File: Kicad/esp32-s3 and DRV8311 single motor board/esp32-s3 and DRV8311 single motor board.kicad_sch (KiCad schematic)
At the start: 41 parts, among them J1 JST SH SM04B, J2 JST SH SM06B, J4 Conn_01x02_Pin, SW1 SW_Push, U5 ESP32-S3, Y1 40mhz

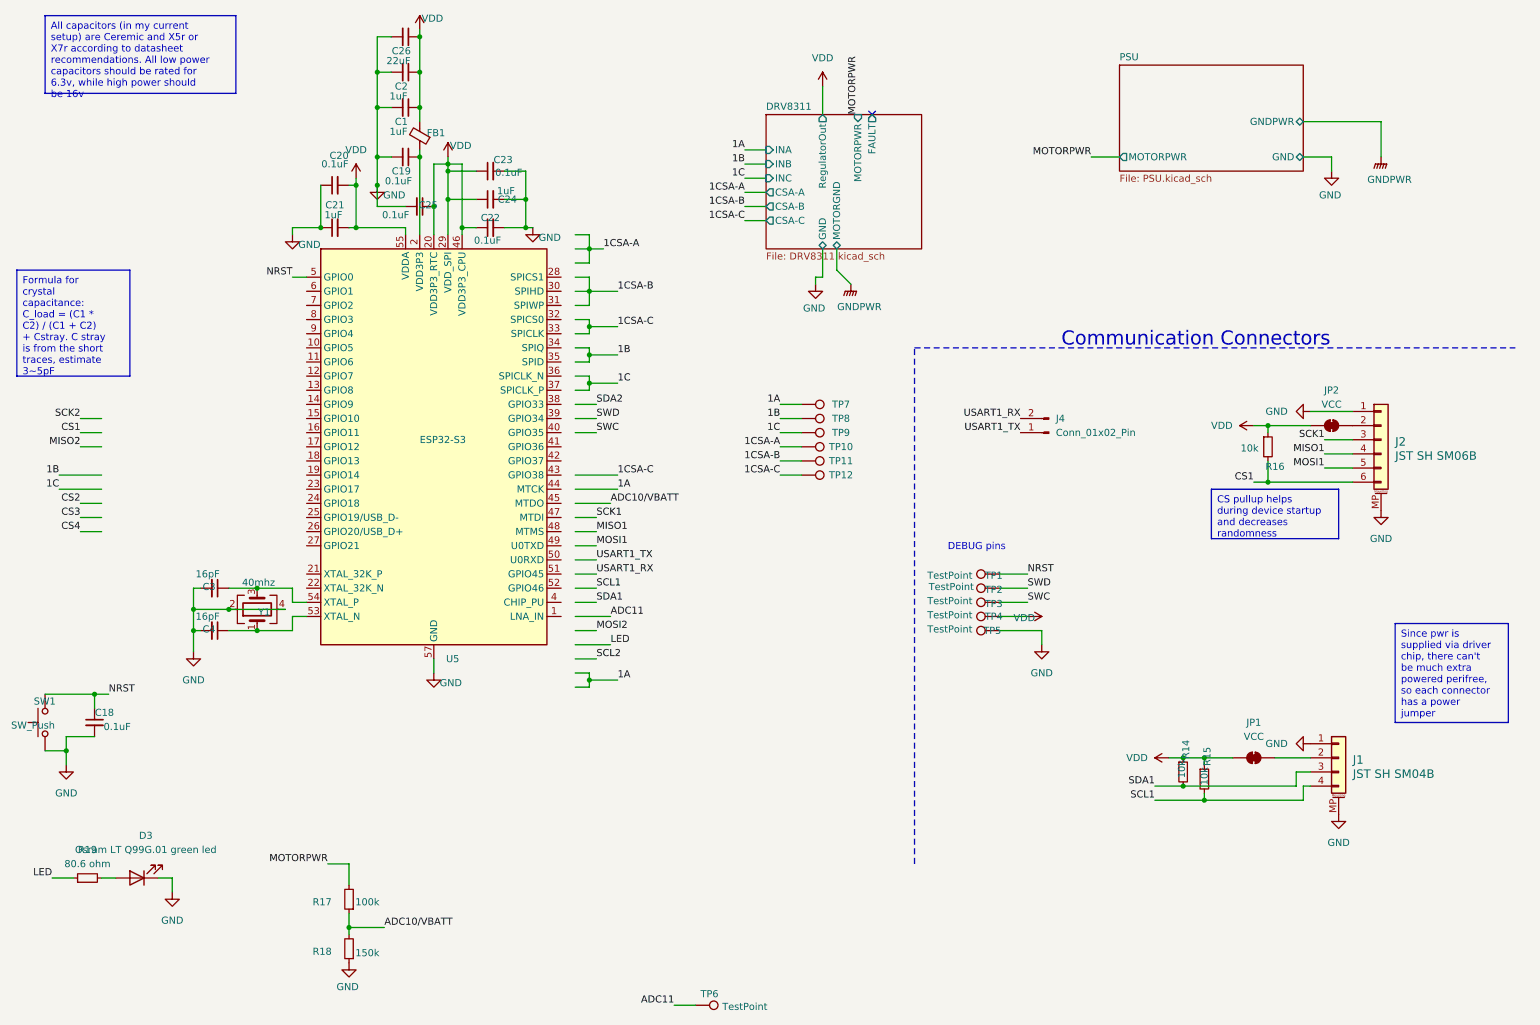
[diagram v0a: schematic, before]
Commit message: Mostly finished draft wiring
I added test points to practically every pin I won't be using regularly. Even if I never use a pin, it is better to have it exposed somehow than to try to solder to a tiny pitch pad
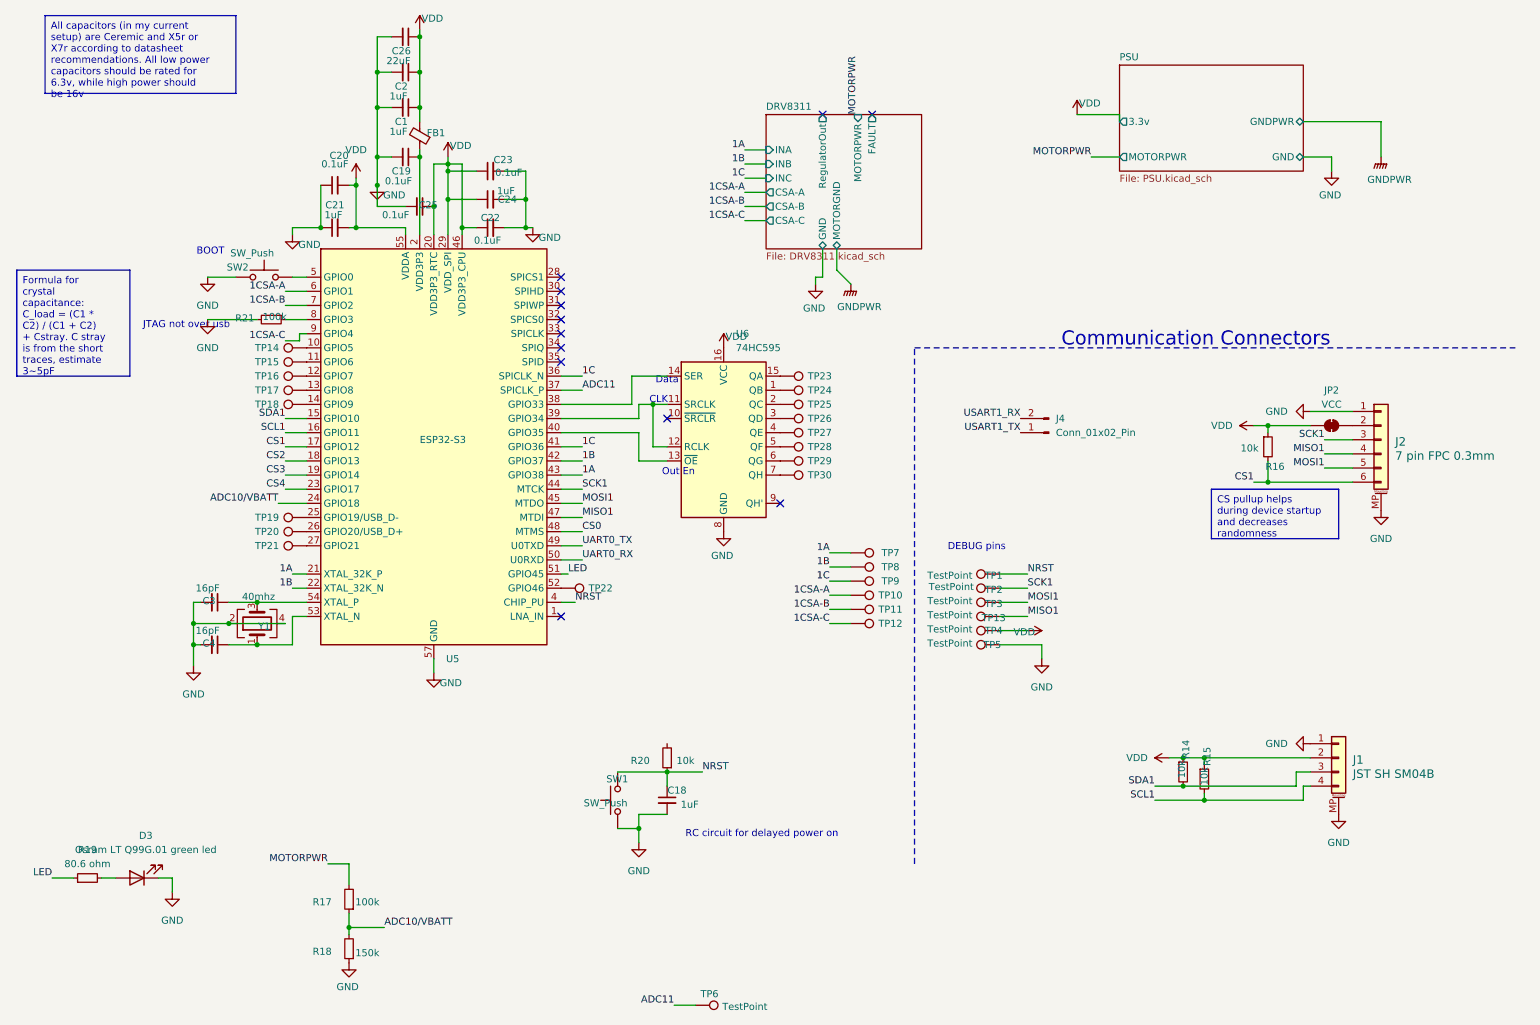
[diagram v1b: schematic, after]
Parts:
- removed JP1: VCC, Jumper:SolderJumper-2_P1.3mm_Bridged_Pad1.0x1.5mm, symbol Jumper:SolderJumper_2_Bridged
- added R20: 10k, Resistor_SMD:R_0603_1608Metric, symbol Device:R_Small
- added R21: 100k, Resistor_SMD:R_0603_1608Metric, symbol Device:R_Small
- added SW2: SW_Push, Button_Switch_SMD:SW_Push_1P1T_NO_CK_KMR2, symbol Switch:SW_Push
- added TP13: TestPoint, TestPoint:TestPoint_Pad_D1.5mm, symbol Connector:TestPoint
- added TP14, TP15, TP16, TP17, TP18, TP19, TP20, TP21, TP22, TP23, TP24, TP25, TP26, TP27, TP28, TP29, TP30: ~, TestPoint:TestPoint_Pad_D1.5mm, symbol Connector:TestPoint
- added U6: 74HC595, symbol 74xx:74HC595
- C18: value 0.1uF -> 1uF
- J2: value JST SH SM06B -> 7 pin FPC 0.3mm
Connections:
- net SWC is gone; now on net MOSI1: TP3.1
- net SWD is gone; now on net SCK1: TP2.1
- net 1A: now also U5.21 (XTAL_32K_P), U5.43 (GPIO38)
- net 1B: now also U5.22 (XTAL_32K_N), U5.42 (GPIO37)
- net 1C: now also U5.36 (SPICLK_N), U5.41 (GPIO36)
- net 1CSA-A: now also U5.6 (GPIO1)
- net 1CSA-B: now also U5.7 (GPIO2)
- net 1CSA-C: now also U5.9 (GPIO4)
- net ADC10/VBATT: now also U5.24 (GPIO18)
- net ADC11: now also U5.37 (SPICLK_P)
- net CS1: now also U5.17 (GPIO12)
- net CS2: now also U5.18 (GPIO13)
- net CS3: now also U5.19 (GPIO14)
- net CS4: now also U5.23 (GPIO17)
- net GND: now also R21.2, SW2.1, U6.8 (GND)
- net LED: now also U5.51 (GPIO45)
- net MISO1: now also U5.47 (MTDI), TP13.1
- net MOSI1: now also U5.45 (MTDO)
- net NRST: now also U5.4 (CHIP_PU), R20.1; no longer U5.5 (GPIO0)
- net SCK1: now also U5.44 (MTCK)
- net SCL1: now also U5.16 (GPIO11)
- net SDA1: now also U5.15 (GPIO10)
- net VDD: now also J1.2 (Pin_2), U6.16 (VCC)
- net at U5.10 (GPIO5): now also TP14.1
- net at U5.11 (GPIO6): now also TP15.1
- net at U5.12 (GPIO7): now also TP16.1
- net at U5.13 (GPIO8): now also TP17.1
- net at U5.14 (GPIO9): now also TP18.1
- net at U5.25 (GPIO19/USB_D-): now also TP19.1
- net at U5.26 (GPIO20/USB_D+): now also TP20.1
- net at U5.27 (GPIO21): now also TP21.1
- net at U5.38 (GPIO33): now also U6.14 (SER)
- net at U5.39 (GPIO34): now also U6.11 (SRCLK), U6.12 (RCLK)
- net at U5.40 (GPIO35): now also U6.13 (~{OE})
- net CS0: now reaches U5.48 (MTMS)
- net UART0_TX: now reaches U5.49 (U0TXD)
- net UART0_RX: now reaches U5.50 (U0RXD)
- net at U5.52 (GPIO46): now also TP22.1
- net at U5.8 (GPIO3): now also R21.1
- new net: TP24.1, U6.1 (QB)
- new net: TP25.1, U6.2 (QC)
- new net: TP30.1, U6.7 (QH)
- new net: TP29.1, U6.6 (QG)
- new net: SW2.2, U5.5 (GPIO0)
- new net: TP23.1, U6.15 (QA)
- new net: TP27.1, U6.4 (QE)
- new net: TP28.1, U6.5 (QF)
- new net: TP26.1, U6.3 (QD)
- no-connect marks 1 -> 12
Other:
- sheet PSU ports: added 3.3v; removed none
- note added: "BOOT"
- note added: "CLK"
- note added: "Data"
- note added: "JTAG not over usb"
- note added: "Out En"
- note added: "RC circuit for delayed power on"
- moved on the sheet: C18, C3, C4, SW1, TP10, TP11, TP12, TP4, TP5, TP7, TP8, TP9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

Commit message: Finished schematic and fixed DRC errors
Now I'm moving on to layout.
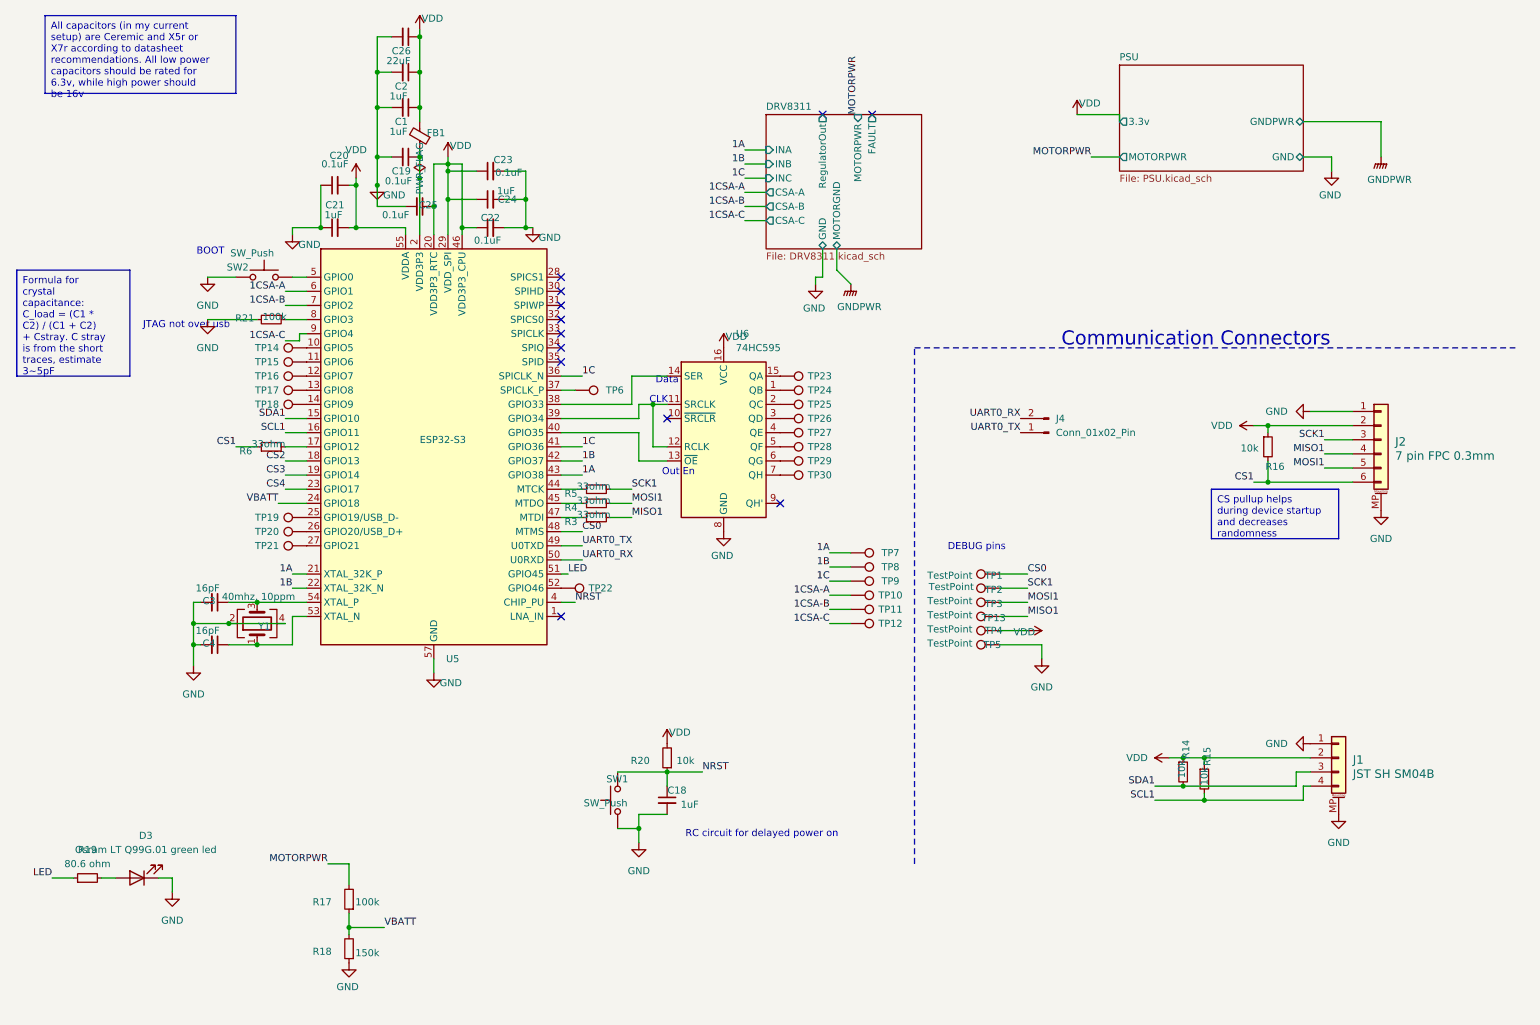
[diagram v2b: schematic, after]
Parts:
- removed JP2: VCC, Jumper:SolderJumper-2_P1.3mm_Bridged_Pad1.0x1.5mm, symbol Jumper:SolderJumper_2_Bridged
- added R3, R4, R5, R6: 33ohm, Resistor_SMD:R_0603_1608Metric, symbol Device:R_Small
- TP6: value TestPoint -> ~
- Y1: value 40mhz -> 40mhz, 10ppm
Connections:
- net USART1_RX is gone; now on net UART0_RX: J4.2 (Pin_2)
- net USART1_TX is gone; now on net UART0_TX: J4.1 (Pin_1)
- net CS0: now also TP1.1
- net CS1: now also R6.1; no longer U5.17 (GPIO12)
- net MISO1: now also R3.2; no longer U5.47 (MTDI)
- net MOSI1: now also R4.2; no longer U5.45 (MTDO)
- net NRST: no longer TP1.1
- net SCK1: now also R5.2; no longer U5.44 (MTCK)
- net VDD: now also J2.2 (Pin_2), R20.2
- net ADC10/VBATT renamed VBATT
- net ADC11: no longer names the net of TP6.1, U5.37 (SPICLK_P)
- new net: R4.1, U5.45 (MTDO)
- new net: R6.2, U5.17 (GPIO12)
- new net: R5.1, U5.44 (MTCK)
- new net: R3.1, U5.47 (MTDI)

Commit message: Wired decoupling capacitors and crystal
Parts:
- U6: footprint (none) -> Package_SO:SO-16_3.9x9.9mm_P1.27mm
- Y1: footprint Crystal:Crystal_SMD_Abracon_ABM8G-4Pin_3.2x2.5mm -> Crystal:Crystal_SMD_3225-4Pin_3.2x2.5mm
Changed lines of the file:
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@@
 			)
 		)
-		(property "Footprint" "Crystal:Crystal_SMD_Abracon_ABM8G-4Pin_3.2x2.5mm"
+		(property "Footprint" "Crystal:Crystal_SMD_3225-4Pin_3.2x2.5mm"
 			(at 58.42 123.19 0)
 			(effects
@@
 			)
 		)
-		(property "Footprint" ""
+		(property "Footprint" "Package_SO:SO-16_3.9x9.9mm_P1.27mm"
 			(at 142.24 88.9 0)
 			(effects

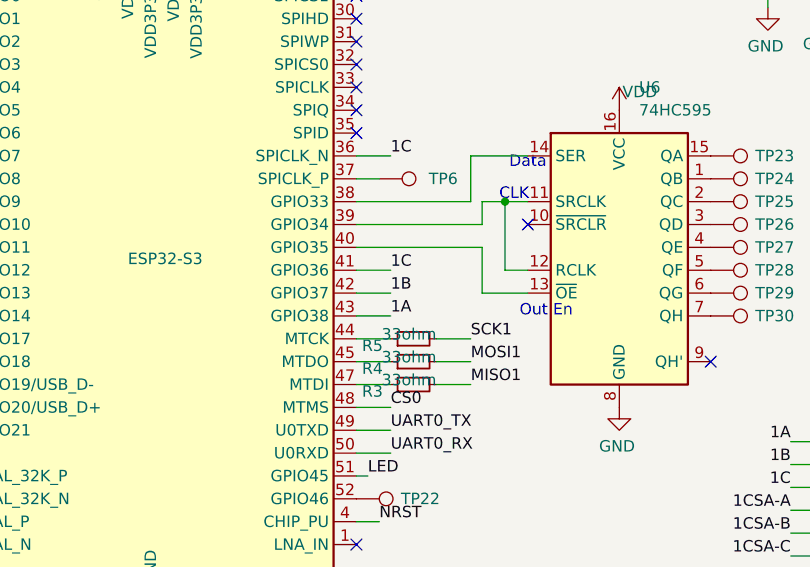
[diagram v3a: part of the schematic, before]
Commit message: Wiring some signal wires and moving power around to accomodate
There are location conflicts left and right! I will eventually get this mess sorted out, but I am wondering about 6 layer boards and blind vias. 4 layers will keep the costs down though!
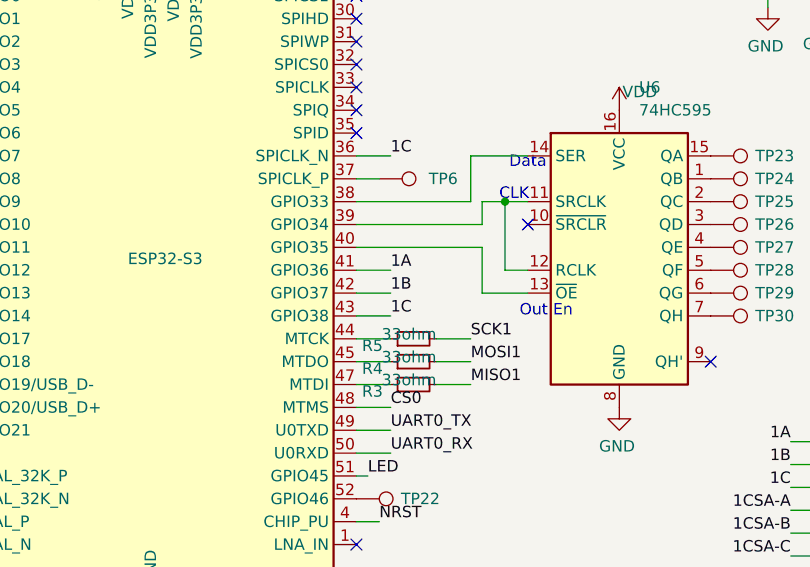
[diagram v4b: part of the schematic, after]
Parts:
- TP1, TP10, TP11, TP12, TP13, TP14, TP15, TP16, TP17, TP18, TP19, TP2, TP20, TP21, TP22, TP23, TP24, TP25, TP26, TP27, TP28, TP29, TP3, TP30, TP4, TP5, TP6, TP7, TP8, TP9: footprint TestPoint:TestPoint_Pad_D1.5mm -> TestPoint:TestPoint_Pad_D1.0mm
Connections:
- net 1A: now also U5.41 (GPIO36); no longer U5.43 (GPIO38)
- net 1C: now also U5.43 (GPIO38); no longer U5.41 (GPIO36)
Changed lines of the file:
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@@
 	)
 	(label "1A"
-		(at 116.84 96.52 0)
+		(at 116.84 91.44 0)
 		(fields_autoplaced yes)
 		(effects
@@
 	)
 	(label "1C"
-		(at 116.84 91.44 0)
+		(at 116.84 96.52 0)
 		(fields_autoplaced yes)
 		(effects
@@
 			)
 		)
-		(property "Footprint" "TestPoint:TestPoint_Pad_D1.5mm"
+		(property "Footprint" "TestPoint:TestPoint_Pad_D1.0mm"
 			(at 152.4 86.36 0)
 			(effects
@@
 			)
 		)
-		(property "Footprint" "TestPoint:TestPoint_Pad_D1.5mm"
+		(property "Footprint" "TestPoint:TestPoint_Pad_D1.0mm"
 			(at 67.31 78.74 0)
 			(effects
@@
 			)
 		)
-		(property "Footprint" "TestPoint:TestPoint_Pad_D1.5mm"
+		(property "Footprint" "TestPoint:TestPoint_Pad_D1.0mm"
 			(at 165.1 125.73 0)
 			(effects
@@
 			)
 		)
-		(property "Footprint" "TestPoint:TestPoint_Pad_D1.5mm"
+		(property "Footprint" "TestPoint:TestPoint_Pad_D1.0mm"
 			(at 115.57 86.36 0)
 			(effects
@@
 			)
 		)
-		(property "Footprint" "TestPoint:TestPoint_Pad_D1.5mm"
+		(property "Footprint" "TestPoint:TestPoint_Pad_D1.0mm"
 			(at 67.31 71.12 0)
 			(effects
@@
 			)
 		)
-		(property "Footprint" "TestPoint:TestPoint_Pad_D1.5mm"
+		(property "Footprint" "TestPoint:TestPoint_Pad_D1.0mm"
 			(at 152.4 88.9 0)
 			(effects
@@
 			)
 		)
-		(property "Footprint" "TestPoint:TestPoint_Pad_D1.5mm"
+		(property "Footprint" "TestPoint:TestPoint_Pad_D1.0mm"
 			(at 67.31 101.6 0)
 			(effects
@@
 			)
 		)
-		(property "Footprint" "TestPoint:TestPoint_Pad_D1.5mm"
+		(property "Footprint" "TestPoint:TestPoint_Pad_D1.0mm"
 			(at 191.77 109.22 0)
 			(effects
@@
 			)
 		)
-		(property "Footprint" "TestPoint:TestPoint_Pad_D1.5mm"
+		(property "Footprint" "TestPoint:TestPoint_Pad_D1.0mm"
 			(at 165.1 120.65 0)
 			(effects
@@
 			)
 		)
-		(property "Footprint" "TestPoint:TestPoint_Pad_D1.5mm"
+		(property "Footprint" "TestPoint:TestPoint_Pad_D1.0mm"
 			(at 67.31 68.58 0)
 			(effects
@@
 			)
 		)
-		(property "Footprint" "TestPoint:TestPoint_Pad_D1.5mm"
+		(property "Footprint" "TestPoint:TestPoint_Pad_D1.0mm"
 			(at 165.1 123.19 0)
 			(effects
@@
 			)
 		)
-		(property "Footprint" "TestPoint:TestPoint_Pad_D1.5mm"
+		(property "Footprint" "TestPoint:TestPoint_Pad_D1.0mm"
 			(at 67.31 104.14 0)
 			(effects
@@
 			)
 		)
-		(property "Footprint" "TestPoint:TestPoint_Pad_D1.5mm"
+		(property "Footprint" "TestPoint:TestPoint_Pad_D1.0mm"
 			(at 67.31 99.06 0)
 			(effects
@@
 			)
 		)
-		(property "Footprint" "TestPoint:TestPoint_Pad_D1.5mm"
+		(property "Footprint" "TestPoint:TestPoint_Pad_D1.0mm"
 			(at 191.77 116.84 0)
 			(effects
@@
 			)
 		)
-		(property "Footprint" "TestPoint:TestPoint_Pad_D1.5mm"
+		(property "Footprint" "TestPoint:TestPoint_Pad_D1.0mm"
 			(at 152.4 101.6 0)
 			(effects
@@
 			)
 		)
-		(property "Footprint" "TestPoint:TestPoint_Pad_D1.5mm"
+		(property "Footprint" "TestPoint:TestPoint_Pad_D1.0mm"
 			(at 113.03 121.92 0)
 			(effects
@@
 			)
 		)
-		(property "Footprint" "TestPoint:TestPoint_Pad_D1.5mm"
+		(property "Footprint" "TestPoint:TestPoint_Pad_D1.0mm"
 			(at 165.1 128.27 0)
 			(effects
@@
 			)
 		)
-		(property "Footprint" "TestPoint:TestPoint_Pad_D1.5mm"
+		(property "Footprint" "TestPoint:TestPoint_Pad_D1.0mm"
 			(at 165.1 115.57 0)
 			(effects
@@
 			)
 		)
-		(property "Footprint" "TestPoint:TestPoint_Pad_D1.5mm"
+		(property "Footprint" "TestPoint:TestPoint_Pad_D1.0mm"
 			(at 67.31 73.66 0)
 			(effects
@@
 			)
 		)
-		(property "Footprint" "TestPoint:TestPoint_Pad_D1.5mm"
+		(property "Footprint" "TestPoint:TestPoint_Pad_D1.0mm"
 			(at 152.4 99.06 0)
 			(effects
@@
 			)
 		)
-		(property "Footprint" "TestPoint:TestPoint_Pad_D1.5mm"
+		(property "Footprint" "TestPoint:TestPoint_Pad_D1.0mm"
 			(at 191.77 121.92 0)
 			(effects
@@
 			)
 		)
-		(property "Footprint" "TestPoint:TestPoint_Pad_D1.5mm"
+		(property "Footprint" "TestPoint:TestPoint_Pad_D1.0mm"
 			(at 152.4 83.82 0)
 			(effects
@@
 			)
 		)
-		(property "Footprint" "TestPoint:TestPoint_Pad_D1.5mm"
+		(property "Footprint" "TestPoint:TestPoint_Pad_D1.0mm"
 			(at 152.4 93.98 0)
 			(effects
@@
 			)
 		)
-		(property "Footprint" "TestPoint:TestPoint_Pad_D1.5mm"
+		(property "Footprint" "TestPoint:TestPoint_Pad_D1.0mm"
 			(at 152.4 96.52 0)
 			(effects
@@
 			)
 		)
-		(property "Footprint" "TestPoint:TestPoint_Pad_D1.5mm"
+		(property "Footprint" "TestPoint:TestPoint_Pad_D1.0mm"
 			(at 191.77 114.3 0)
 			(effects
@@
 			)
 		)
-		(property "Footprint" "TestPoint:TestPoint_Pad_D1.5mm"
+		(property "Footprint" "TestPoint:TestPoint_Pad_D1.0mm"
 			(at 67.31 76.2 0)
 			(effects
@@
 			)
 		)
-		(property "Footprint" "TestPoint:TestPoint_Pad_D1.5mm"
+		(property "Footprint" "TestPoint:TestPoint_Pad_D1.0mm"
 			(at 152.4 91.44 0)
 			(effects
@@
 			)
 		)
-		(property "Footprint" "TestPoint:TestPoint_Pad_D1.5mm"
+		(property "Footprint" "TestPoint:TestPoint_Pad_D1.0mm"
 			(at 165.1 118.11 0)
 			(effects
@@
 			)
 		)
-		(property "Footprint" "TestPoint:TestPoint_Pad_D1.5mm"
+		(property "Footprint" "TestPoint:TestPoint_Pad_D1.0mm"
 			(at 191.77 111.76 0)
 			(effects
@@
 			)
 		)
-		(property "Footprint" "TestPoint:TestPoint_Pad_D1.5mm"
+		(property "Footprint" "TestPoint:TestPoint_Pad_D1.0mm"
 			(at 191.77 119.38 0)
 			(effects

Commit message: Wire mess progress
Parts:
- U6: footprint Package_SO:SO-16_3.9x9.9mm_P1.27mm -> Package_DFN_QFN:DHVQFN-16-1EP_2.5x3.5mm_P0.5mm_EP1x2mm
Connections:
- net GND: now also U6.17 (Pad)
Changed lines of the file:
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@@
 			)
 		)
-		(property "Footprint" "Package_SO:SO-16_3.9x9.9mm_P1.27mm"
+		(property "Footprint" "Package_DFN_QFN:DHVQFN-16-1EP_2.5x3.5mm_P0.5mm_EP1x2mm"
 			(at 142.24 88.9 0)
 			(effects
@@
 		(pin "10"
 		)
+		(pin "17"
+		)
 		(instances
